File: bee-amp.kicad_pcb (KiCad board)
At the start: 2 copper layers, 29 x 53.3 mm, 35 parts, among them J1 Conn_01x02_Male, J10 Conn_01x02, J2 Conn_01x02_Male, J3 Conn_01x02_Male, J4 Conn_01x02_Male, J7 Conn_01x03, J8 Conn_01x02, J9 Conn_01x02, U1 OP07

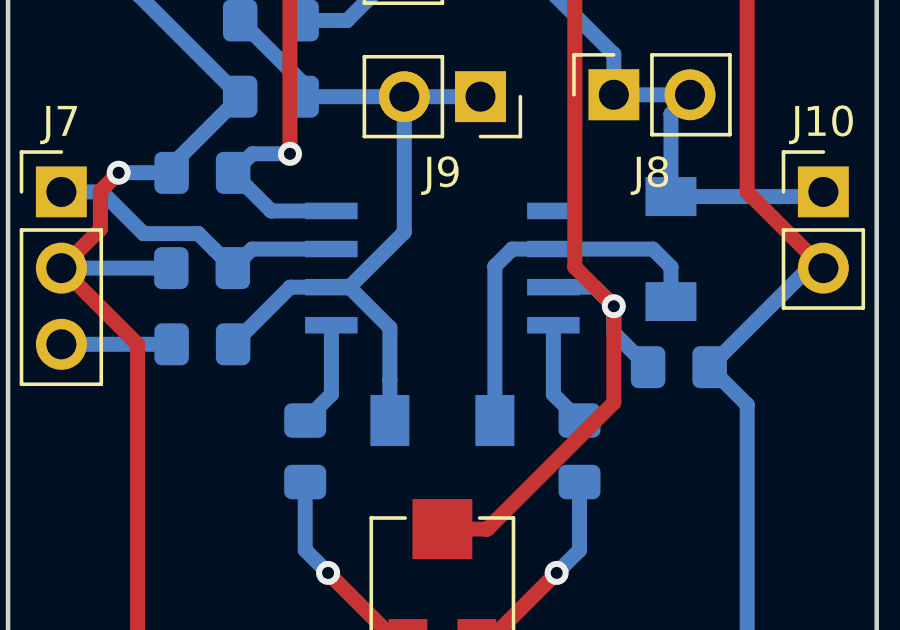
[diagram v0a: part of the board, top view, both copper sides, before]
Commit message: Replace SO package by SOIC. Fixes #1.
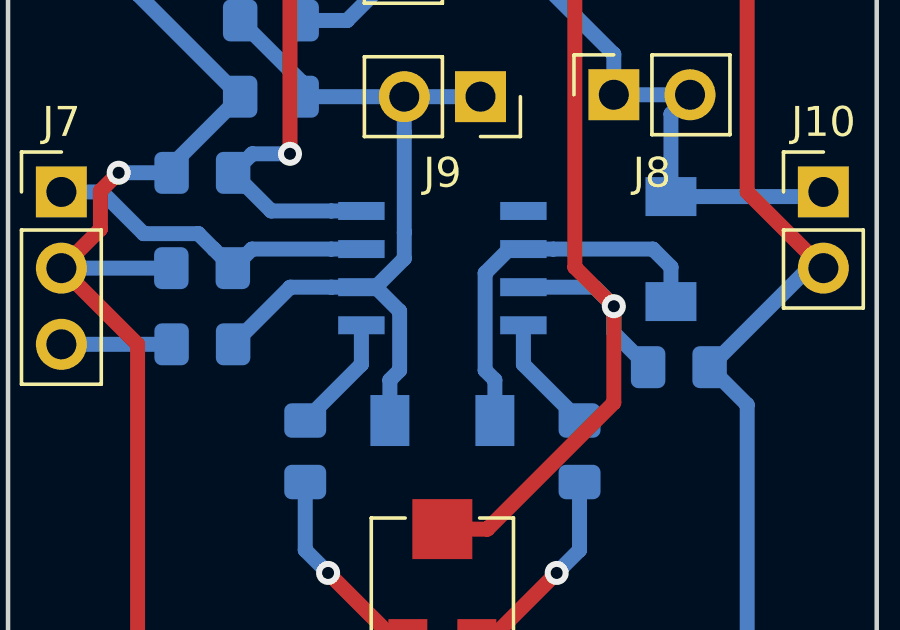
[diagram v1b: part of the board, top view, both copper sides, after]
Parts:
- D1, D2: value LL4148 -> 1N4148
- R1, R5: value R -> 10k
- R2: value R -> 0
- R6: value R -> 1,1k
- U1: footprint Package_SO:SO-8_5.3x6.2mm_P1.27mm -> Package_SO:SOIC-8_3.9x4.9mm_P1.27mm
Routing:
- net V-: track 46.2 -> 47.2 mm
- net V+: track 64.9 -> 65.9 mm
- net Net-(J7-Pad1): track 10.3 -> 11.2 mm
- net Net-(D1-Pad1): track 12.6 -> 13.3 mm

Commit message: Relabel as bee specific.
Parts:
- H1, H2: footprint Symbol-emt:Text_U_B+_Silkscreen -> Symbol-bee:Text_U_B+_Silkscreen
- H13: footprint Symbol-emt:EMT-Logo_5.1x2.5mm_Silkscreen -> Symbol-bee:EMT-Logo_5.1x2.5mm_Silkscreen
- H14: footprint Symbol-emt:BEE-Logo_Silkscreen_small -> Symbol-bee:BEE-Logo_Silkscreen_small
- H3, H4: footprint Symbol-emt:Text_U_B-_Silkscreen -> Symbol-bee:Text_U_B-_Silkscreen
- H5, H6: footprint Symbol-emt:Text_U_B2_Silkscreen -> Symbol-bee:Text_U_B2_Silkscreen
- H7, H8: footprint Symbol-emt:Symbol_GND_Silkscreen -> Symbol-bee:Symbol_GND_Silkscreen
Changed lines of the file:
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@@
     )
   )
-  (module Symbol-emt:Text_U_B+_Silkscreen (layer F.Cu)
+  (module Symbol-bee:Text_U_B+_Silkscreen (layer F.Cu)
     (at 75.184 91.44)
     (descr "Voltage Label Betriebsspannung")
@@
     )
   )
-  (module Symbol-emt:Text_U_B+_Silkscreen (layer F.Cu)
+  (module Symbol-bee:Text_U_B+_Silkscreen (layer F.Cu)
     (at 101.092 91.44)
     (descr "Voltage Label Betriebsspannung")
@@
     )
   )
-  (module Symbol-emt:Text_U_B-_Silkscreen (layer F.Cu)
+  (module Symbol-bee:Text_U_B-_Silkscreen (layer F.Cu)
     (at 101.092 93.98)
     (descr "Voltage Label Betriebsspannung")
@@
     )
   )
-  (module Symbol-emt:Text_U_B-_Silkscreen (layer F.Cu)
+  (module Symbol-bee:Text_U_B-_Silkscreen (layer F.Cu)
     (at 75.184 93.98)
     (descr "Voltage Label Betriebsspannung")
@@
     )
   )
-  (module Symbol-emt:Text_U_B2_Silkscreen (layer F.Cu)
+  (module Symbol-bee:Text_U_B2_Silkscreen (layer F.Cu)
     (at 75.184 137.16)
     (descr "Voltage Label Betriebsspannung")
@@
     )
   )
-  (module Symbol-emt:Text_U_B2_Silkscreen (layer F.Cu)
+  (module Symbol-bee:Text_U_B2_Silkscreen (layer F.Cu)
     (at 101.092 137.16)
     (descr "Voltage Label Betriebsspannung")
@@
     )
   )
-  (module Symbol-emt:Symbol_GND_Silkscreen (layer F.Cu)
+  (module Symbol-bee:Symbol_GND_Silkscreen (layer F.Cu)
     (at 75.692 139.7)
     (descr "Symbol GND")
@@
     (fp_line (start -0.5 0.8) (end 0.5 0.8) (layer F.SilkS) (width 0.25))
   )
-  (module Symbol-emt:Symbol_GND_Silkscreen (layer F.Cu)
+  (module Symbol-bee:Symbol_GND_Silkscreen (layer F.Cu)
     (at 102.108 139.7)
     (descr "Symbol GND")
@@
       (net 1 GND))
   )
-  (module Symbol-emt:EMT-Logo_5.1x2.5mm_Silkscreen (layer F.Cu)
+  (module Symbol-bee:EMT-Logo_5.1x2.5mm_Silkscreen (layer F.Cu)
     (at 86.106 94.234)
     (descr EMT-Logo)
@@
       (xy 1.243014 -1.158797)) (layer F.SilkS) (width 0.01))
   )
-  (module Symbol-emt:BEE-Logo_Silkscreen_small (layer F.Cu)
+  (module Symbol-bee:BEE-Logo_Silkscreen_small (layer F.Cu)
     (at 91.948 94.742)
     (descr BEE-Logo)
